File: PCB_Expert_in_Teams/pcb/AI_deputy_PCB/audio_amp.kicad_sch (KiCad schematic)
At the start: 0 parts

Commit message: updating repo from desktop
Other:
- company: (none) -> Area 42 & Albers-Online Psykologi
- title: (none) -> AI Deputy
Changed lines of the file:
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@@
 	(generator_version "9.0")
 	(paper "A4")
+	(title_block
+		(title "AI Deputy")
+		(date "2025-09-24")
+		(rev "v0.1")
+		(company "Area 42 & Albers-Online Psykologi")
+		(comment 1 "SDU")
+		(comment 2 "Expert In Teams Semester Project")
+	)
 )

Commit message: progress on PCB + matlab calculations
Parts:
- added C19, C20, C21, C22, C23, C25: 0.1u, Capacitor_SMD:C_0805_2012Metric_Pad1.18x1.45mm_HandSolder, symbol Device:C
- added C24, C26: 1u, Capacitor_SMD:C_0805_2012Metric_Pad1.18x1.45mm_HandSolder, symbol Device:C
- added IC4, IC5: IS31AP2005-SLS2-TR, EXT_AI_DEPUTY_Library:SOP65P490X110-8N, symbol IS31AP2005-SLS2-TR:IS31AP2005-SLS2-TR
- added J13, J14: Conn_01x02_Socket, Connector_JST:JST_XH_S2B-XH-A-1_1x02_P2.50mm_Horizontal, symbol Connector:Conn_01x02_Socket
- added J8: Conn_01x04_Socket, Connector_JST:JST_XH_S4B-XH-A-1_1x04_P2.50mm_Horizontal, symbol Connector:Conn_01x04_Socket
- added R10, R11, R12, R9: 150k, Resistor_SMD:R_0805_2012Metric_Pad1.20x1.40mm_HandSolder, symbol Device:R
- added R13, R14: 100k, Resistor_SMD:R_0805_2012Metric_Pad1.20x1.40mm_HandSolder, symbol Device:R
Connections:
- new net: IC5.4 (IN-), R12.1
- new net: C22.2, R12.2
- new net: IC4.1 (SDB), R14.1
- new net: C20.2, R10.1
- new net: IC4.3 (IN+), R10.2
- new net: IC4.4 (IN-), R9.1
- new net: IC4.5 (OUT+), J13.2 (Pin_2)
- new net: IC4.8 (OUT-), J13.1 (Pin_1)
- new net: IC5.1 (SDB), R13.1
- new net: IC5.3 (IN+), R11.2
- new net: IC5.5 (OUT+), J14.2 (Pin_2)
- new net: IC5.8 (OUT-), J14.1 (Pin_1)
- new net: C19.2, R9.2
- new net: C21.2, R11.1
- new net +3V3: C23.2, C24.2, C25.2, C26.2, IC4.6 (VCC), IC5.6 (VCC), J8.2 (Pin_2), R13.2, R14.2
- new net GND: C20.1, C21.1, C23.1, C24.1, C25.1, C26.1, IC4.7 (GND), IC5.7 (GND), J8.1 (Pin_1)
- new net Signal Left: C19.1, J8.3 (Pin_3)
- new net Signal Right: C22.1, J8.4 (Pin_4)
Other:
- note added: "Left Amplifier"
- note added: "Need to build DAC circuit if i dont want to use 8bit DAC on ESP32"
- note added: "Right Amplifier"
- note added: "Speaker Output Left"
- note added: "Speaker Output Right"

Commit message: update schematic from desktop
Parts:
- added C41, C53, C59, C61: 0.1u, Capacitor_SMD:C_0805_2012Metric_Pad1.18x1.45mm_HandSolder, symbol Device:C
- added C42, C52, C58, C60: 10u, Capacitor_SMD:CP_Elec_4x5.4, symbol Device:C_Polarized_US
- added C54, C55, C56, C57: 2.2u, Capacitor_SMD:C_0805_2012Metric_Pad1.18x1.45mm_HandSolder, symbol Device:C
- added IC9: PCM5102APWR, SOP65P640X120-20N, symbol DAC-PCM510:PCM5102APWR
- added R41: 10k, Resistor_SMD:R_0805_2012Metric_Pad1.20x1.40mm_HandSolder, symbol Device:R
- added R42, R43: 470, Resistor_SMD:R_0805_2012Metric_Pad1.20x1.40mm_HandSolder, symbol Device:R
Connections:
- net +3V3: now also C41.2, C42.1, C52.1, C53.2, C58.1, C59.2, IC9.1 (CPVDD), IC9.20 (DVDD), IC9.9 (AGND), R41.2
- net GND: now also C41.1, C42.2, C56.2, C57.2, C58.2, C59.1, C60.2, C61.1, IC9.10 (DEMP), IC9.11 (FLT), IC9.16 (FMT), IC9.19 (DGND), IC9.8 (AVDD)
- net Signal Left: now also C57.1, R43.2
- net Signal Right: now also C56.1, R42.2
- new net: C52.2, C53.1, C54.1, C55.1, IC9.2 (CAPP), IC9.3 (CPGND)
- new net: C60.1, C61.2, IC9.18 (LDOO)
- new net: C54.2, IC9.4 (CAPM)
- new net: C55.2, IC9.5 (VNEG)
- new net DAC_BCK: IC9.13 (BCK)
- new net DAC_DIN: IC9.14 (DIN)
- new net DAC_LRCK: IC9.15 (LRCK)
- new net MUTE: IC9.17 (XSMT), R41.1
- new net OUTL: IC9.6 (OUTL), R43.1
- new net OUTR: IC9.7 (OUTR), R42.1
- no-connect marks 0 -> 1
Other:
- note removed: "Need to build DAC circuit if i dont want to use 8bit DAC on ESP32"
- moved on the sheet: C19, C20, C21, C22, C23, C24, C25, C26, IC4, IC5, J13, J14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

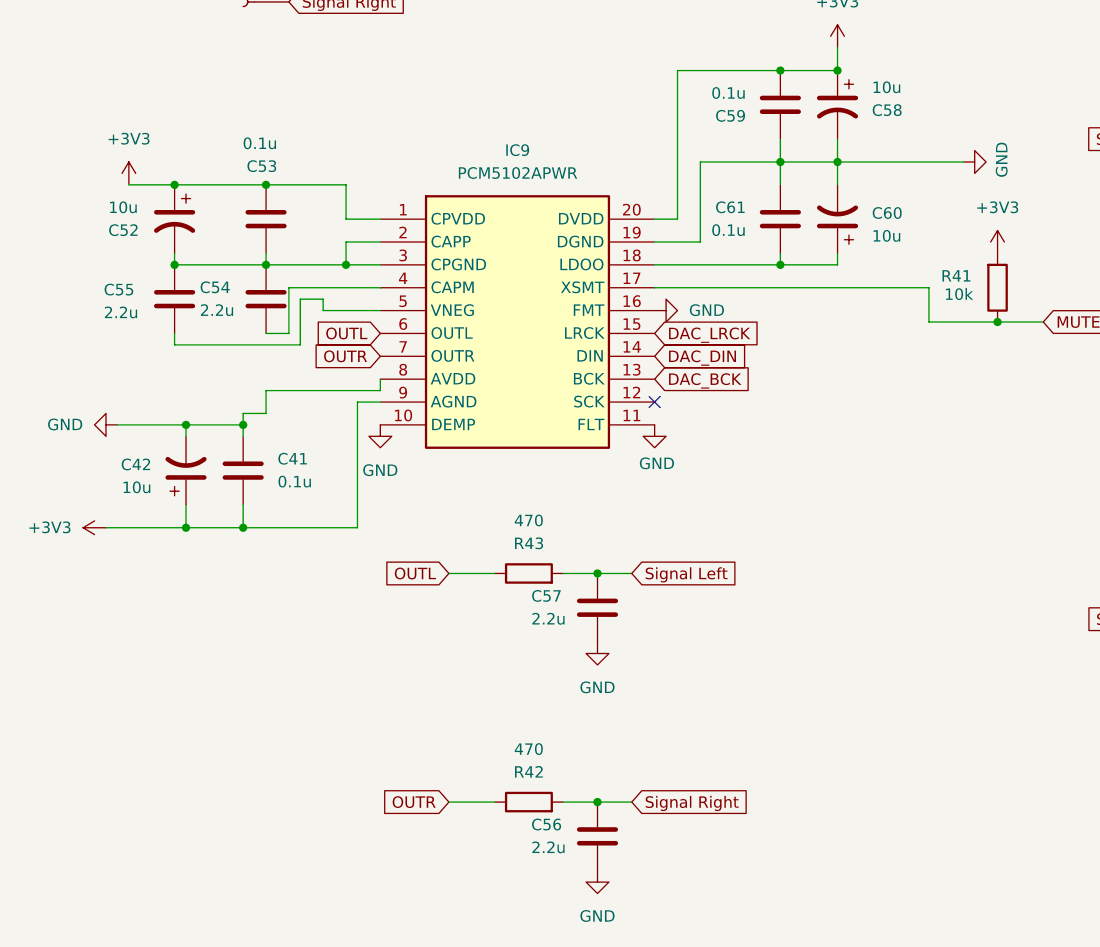
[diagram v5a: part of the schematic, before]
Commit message: pcb updates from desktop with schematic fix
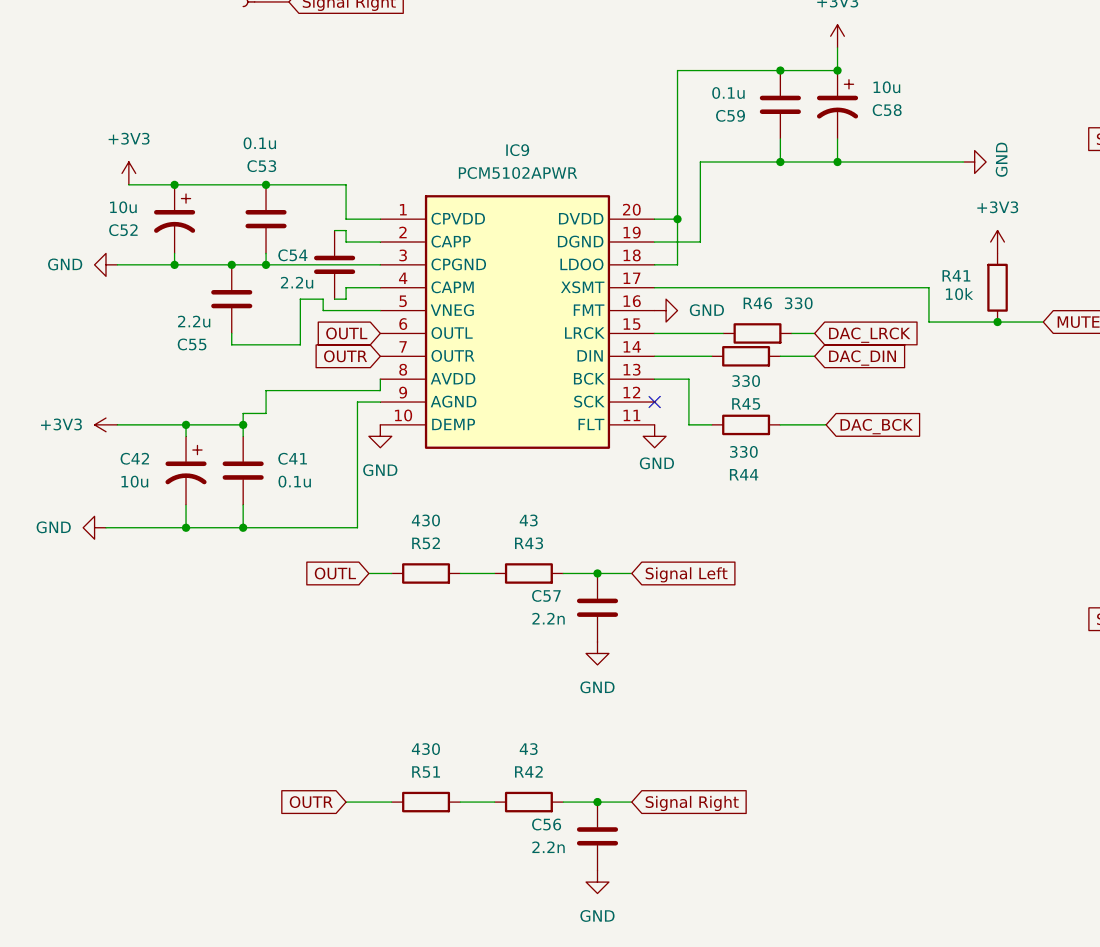
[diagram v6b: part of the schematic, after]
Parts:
- removed C60: 10u, Capacitor_SMD:CP_Elec_4x5.4, symbol Device:C_Polarized_US
- removed C61: 0.1u, Capacitor_SMD:C_0805_2012Metric_Pad1.18x1.45mm_HandSolder, symbol Device:C
- added R44, R45, R46: 330, Resistor_SMD:R_0805_2012Metric_Pad1.20x1.40mm_HandSolder, symbol Device:R
- added R51, R52: 430, Resistor_SMD:R_0805_2012Metric_Pad1.20x1.40mm_HandSolder, symbol Device:R
- C56, C57: value 2.2u -> 2.2n; footprint Capacitor_SMD:C_0805_2012Metric_Pad1.18x1.45mm_HandSolder -> Capacitor_SMD:C_0201_0603Metric_Pad0.64x0.40mm_HandSolder
- R42, R43: value 470 -> 43
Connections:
- net +3V3: now also C41.1, IC9.18 (LDOO), IC9.8 (AVDD); no longer C41.2, IC9.9 (AGND)
- net DAC_BCK: now also R44.2; no longer IC9.13 (BCK)
- net DAC_DIN: now also R45.2; no longer IC9.14 (DIN)
- net DAC_LRCK: now also R46.2; no longer IC9.15 (LRCK)
- net GND: now also C41.2, C52.2, C53.1, C55.1, IC9.3 (CPGND), IC9.9 (AGND); no longer C41.1, IC9.8 (AVDD)
- net OUTL: now also R52.1; no longer R43.1
- net OUTR: now also R51.1; no longer R42.1
- new net: IC9.13 (BCK), R44.1
- new net: R42.1, R51.2
- new net: IC9.14 (DIN), R45.1
- new net: IC9.15 (LRCK), R46.1
- new net: C54.1, IC9.2 (CAPP)
- new net: R43.1, R52.2
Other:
- moved on the sheet: C54, C55

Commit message: before saturday work
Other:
- note added: "Delete Connectors add pads instead"
- note added: "i2S should be same trace length"
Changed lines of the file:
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@@
+		)
+	)
+	(text "Delete Connectors add pads instead \n"
+		(exclude_from_sim no)
+		(at 260.604 77.724 0)
+		(effects
+			(font
+				(size 1.27 1.27)
+			)
 		)
 	)
@@
 		(exclude_from_sim no)
 		(at 180.848 35.56 0)
+		(effects
+			(font
+				(size 1.27 1.27)
+			)
+		)
+	)
+	(text "i2S should be same trace length\n"
+		(exclude_from_sim no)
+		(at 114.808 89.154 0)
 		(effects
 			(font
@@
 				(justify right)
 				(hide yes)
+			)
+		)
+	)
+	(rule_area
+		(polyline
+			(pts
+				(xy 241.3 73.66) (xy 280.67 73.66) (xy 280.67 82.55) (xy 241.3 82.55)
+			)
+			(stroke
+				(width 0)
+				(type dash)
+			)
+			(fill
+				(type none)
 			)
 		)
@@
 			)
 		)
-		(property "Datasheet" "https://componentsearchengine.com/Datasheets/2/PCM5102APWR.pdf"
+		(property "Datasheet" "https://www.ti.com/lit/ds/symlink/pcm5102a.pdf?ts=1764226174169&ref_url=https%253A%252F%252Fwww.ti.com%252Fproduct%252FPCM5102A"
 			(at 80.01 264.77 0)
 			(effects

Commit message: update after lab session with gustav saturday
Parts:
- added C43: 0.1u, Capacitor_SMD:C_0805_2012Metric_Pad1.18x1.45mm_HandSolder, symbol Device:C
- added C60: 10u, Capacitor_SMD:CP_Elec_4x5.4, symbol Device:C_Polarized_US
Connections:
- net +3V3: no longer IC9.18 (LDOO)
- net GND: now also C43.1, C60.2
- new net: C43.2, C60.1, IC9.18 (LDOO)
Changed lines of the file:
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@@
 	)
 	(junction
+		(at 97.79 74.93)
+		(diameter 0)
+		(color 0 0 0 0)
+	)
+	(junction
 		(at 31.75 92.71)
 		(diameter 0)
@@
 	)
 	(junction
-		(at 86.36 69.85)
-		(diameter 0)
-		(color 0 0 0 0)
-	)
-	(junction
 		(at 40.64 74.93)
 		(diameter 0)
@@
 	(wire
 		(pts
+			(xy 97.79 74.93) (xy 97.79 73.66)
+		)
+		(stroke
+			(width 0)
+			(type default)
+		)
+	)
+	(wire
+		(pts
 			(xy 104.14 60.96) (xy 104.14 63.5)
 		)
@@
 	(wire
 		(pts
-			(xy 83.82 74.93) (xy 86.36 74.93)
+			(xy 83.82 74.93) (xy 97.79 74.93)
 		)
 		(stroke
@@
 	(wire
 		(pts
+			(xy 104.14 74.93) (xy 104.14 73.66)
+		)
+		(stroke
+			(width 0)
+			(type default)
+		)
+	)
+	(wire
+		(pts
 			(xy 49.53 77.47) (xy 53.34 77.47)
 		)
@@
 	(wire
 		(pts
-			(xy 86.36 74.93) (xy 86.36 69.85)
-		)
-		(stroke
-			(width 0)
-			(type default)
-		)
-	)
-	(wire
-		(pts
 			(xy 40.64 74.93) (xy 36.83 74.93)
 		)
@@
 	(wire
 		(pts
+			(xy 104.14 63.5) (xy 104.14 66.04)
+		)
+		(stroke
+			(width 0)
+			(type default)
+		)
+	)
+	(wire
+		(pts
 			(xy 38.1 91.44) (xy 38.1 92.71)
 		)
@@
 	(wire
 		(pts
+			(xy 97.79 63.5) (xy 97.79 66.04)
+		)
+		(stroke
+			(width 0)
+			(type default)
+		)
+	)
+	(wire
+		(pts
 			(xy 36.83 83.82) (xy 44.45 83.82)
 		)
@@
 	(wire
 		(pts
+			(xy 97.79 74.93) (xy 104.14 74.93)
+		)
+		(stroke
+			(width 0)
+			(type default)
+		)
+	)
+	(wire
+		(pts
 			(xy 40.64 91.44) (xy 40.64 88.9)
 		)
@@
 	)
 	(symbol
+		(lib_id "Device:C_Polarized_US")
+		(at 104.14 69.85 180)
+		(unit 1)
+		(exclude_from_sim no)
+		(in_bom yes)
+		(on_board yes)
+		(dnp no)
+		(property "Reference" "C60"
+			(at 107.95 69.2149 0)
+			(effects
+				(font
+					(size 1.27 1.27)
+				)
+				(justify right)
+			)
+		)
+		(property "Value" "10u"
+			(at 107.95 71.7549 0)
+			(effects
+				(font
+					(size 1.27 1.27)
+				)
+				(justify right)
+			)
+		)
+		(property "Footprint" "Capacitor_SMD:CP_Elec_4x5.4"
+			(at 104.14 69.85 0)
+			(effects
+				(font
+					(size 1.27 1.27)
+				)
+				(hide yes)
+			)
+		)
+		(property "Datasheet" "~"
+			(at 104.14 69.85 0)
+			(effects
+				(font
+					(size 1.27 1.27)
+				)
+				(hide yes)
+			)
+		)
+		(property "Description" "Polarized capacitor, US symbol"
+			(at 104.14 69.85 0)
+			(effects
+				(font
+					(size 1.27 1.27)
+				)
+				(hide yes)
+			)
+		)
+		(pin "2"
+		)
+		(pin "1"
+		)
+		(instances
+			(project "AI_deputy_PCB"
+				(path "/3784b751-4d5b-4452-8288-14e483e1cb48/4600983a-86b8-49e8-8db6-b0ddbc3ab361"
+					(reference "C60")
+					(unit 1)
+				)
+			)
+		)
+	)
+	(symbol
 		(lib_id "Device:C")
 		(at 147.32 50.8 90)
@@
 					(unit 1)
 				)
+			)
+		)
+	)
+	(symbol
+		(lib_id "Device:C")
+		(at 97.79 69.85 0)
+		(mirror y)
+		(unit 1)
+		(exclude_from_sim no)
+		(in_bom yes)
+		(on_board yes)
+		(dnp no)
+		(property "Reference" "C43"
+			(at 93.98 68.5799 0)
+			(effects
+				(font
+					(size 1.27 1.27)
+				)
+				(justify left)
+			)
+		)
+		(property "Value" "0.1u"
+			(at 93.98 71.1199 0)
+			(effects
+				(font
+					(size 1.27 1.27)
+				)
+				(justify left)
+			)
+		)
+		(property "Footprint" "Capacitor_SMD:C_0805_2012Metric_Pad1.18x1.45mm_HandSolder"
+			(at 96.8248 73.66 0)
+			(effects
+				(font
+					(size 1.27 1.27)
+				)
+				(hide yes)
+			)
+		)
+		(property "Datasheet" "~"
+			(at 97.79 69.85 0)
+			(effects
+				(font
+					(size 1.27 1.27)
+				)
+				(hide yes)
+			)
+		)
+		(property "Description" "Unpolarized capacitor"
+			(at 97.79 69.85 0)
+			(effects
+				(font
+					(size 1.27 1.27)
+				)
+				(hide yes)
+			)
+		)
+		(pin "1"
+		)
+		(pin "2"
+		)
+		(instances
+			(project "AI_deputy_PCB"
+				(path "/3784b751-4d5b-4452-8288-14e483e1cb48/4600983a-86b8-49e8-8db6-b0ddbc3ab361"
+					(reference "C43")
+					(unit 1)
+				)
